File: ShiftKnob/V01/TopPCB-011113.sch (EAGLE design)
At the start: 6 parts, among them IC1 74HC595D

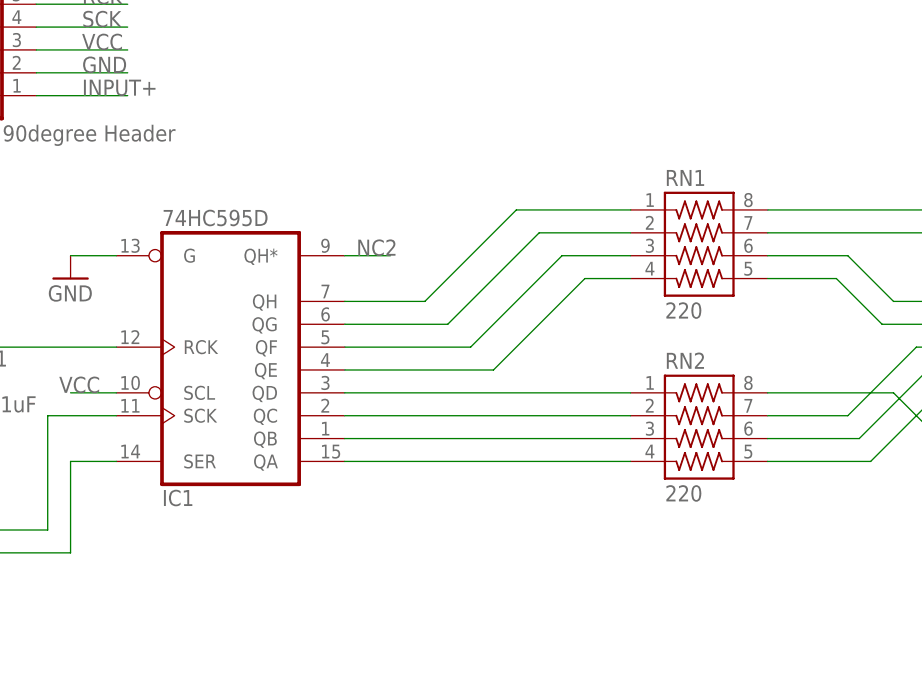
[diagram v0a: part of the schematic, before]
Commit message: name components, add silk screen labels, copy name-date-logo to bottom layer, increase board diameter to 33mm
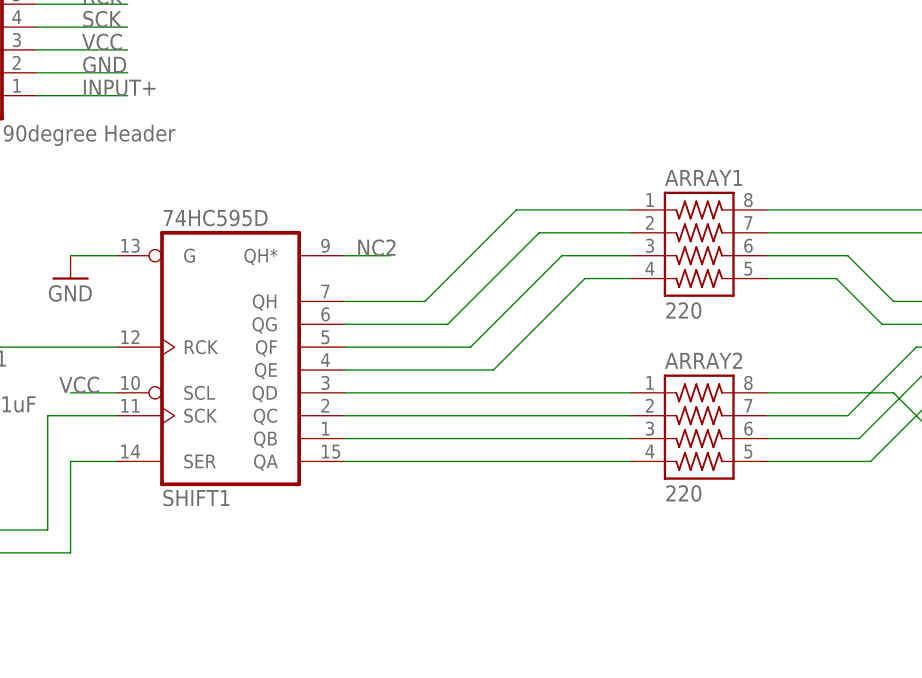
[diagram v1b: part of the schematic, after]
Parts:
- renumbered IC1 to SHIFT1, RN1 to ARRAY1, RN2 to ARRAY2, U$1 to 7SEGMENT

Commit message: change 6 pin connector to match bottomPCB. run DRC and correct issues. move dimension callout to Document layer.
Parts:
- JP1: device SparkFun-Connectors:M06POGOPIN_HOLES_ONLY -> SparkFun-Connectors:M06SIP
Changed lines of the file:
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@@
 <part name="FRAME1" library="frames" deviceset="FRAME_A_L" device=""/>
 <part name="GND3" library="SparkFun-Aesthetics" deviceset="GND" device=""/>
-<part name="JP1" library="SparkFun-Connectors" deviceset="M06" device="POGOPIN_HOLES_ONLY" value="6 PIN 90degree Header"/>
+<part name="JP1" library="SparkFun-Connectors" deviceset="M06" device="SIP" value="6 PIN 90degree Header"/>
 <part name="C1" library="SparkFun-Capacitors" deviceset="CAP" device="0402-CAP" value="0.1uF"/>
 <part name="GND4" library="SparkFun-Aesthetics" deviceset="GND" device=""/>

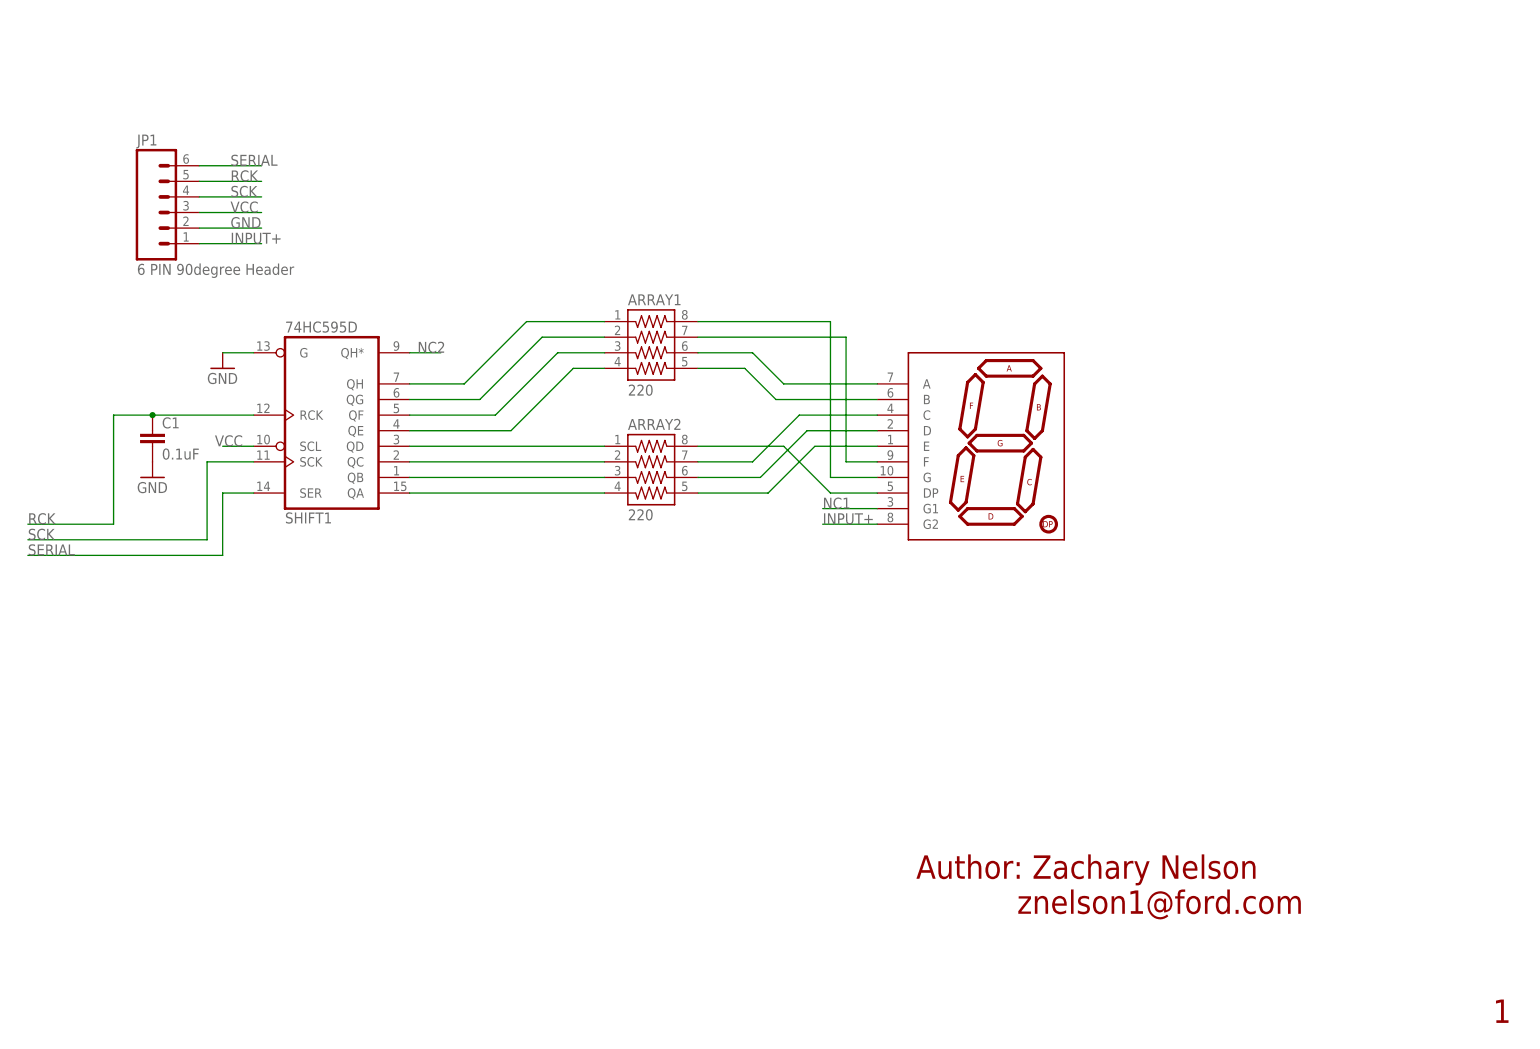
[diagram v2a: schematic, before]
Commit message: update schematics with new Ford frame.
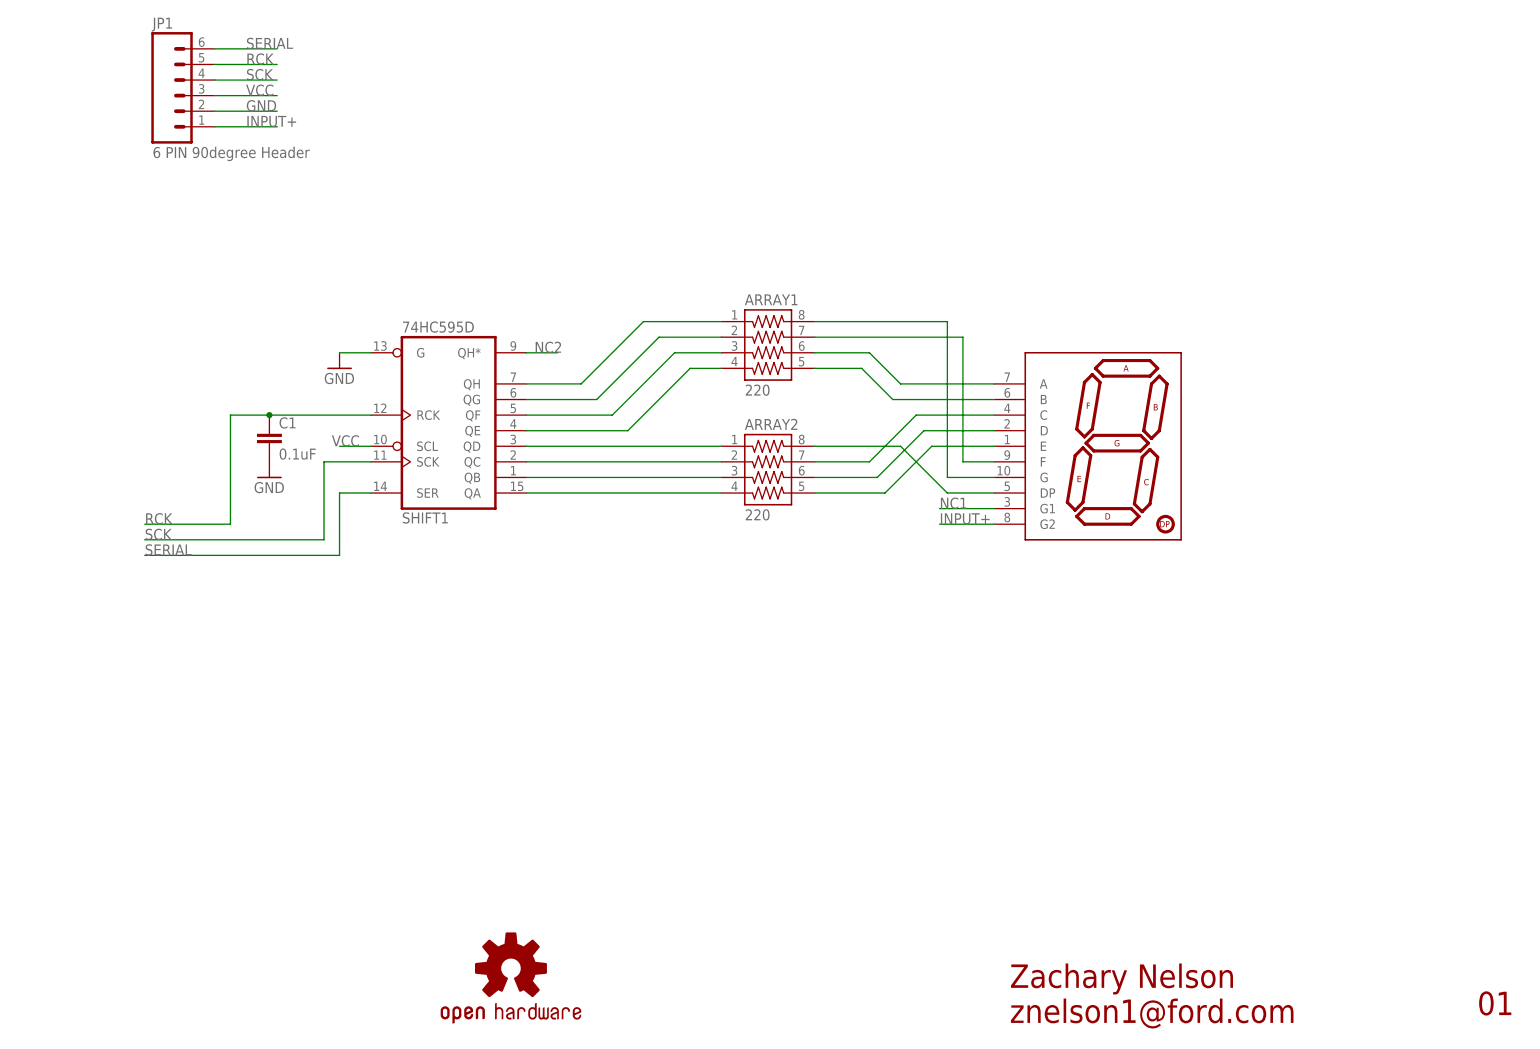
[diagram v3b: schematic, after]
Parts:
- added LOGO1: OSHW-LOGOS, SparkFun-Aesthetics:OSHW-LOGOS
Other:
- note added: "01"
- note added: "Zachary Nelson znelson1@ford.com"
- note removed: "1"
- note removed: "Author: Zachary Nelson znelson1@ford.com"
- moved on the sheet: ARRAY1, ARRAY2, C1, JP1, SHIFT1

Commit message: update with new frames and printed drawings for assembly.
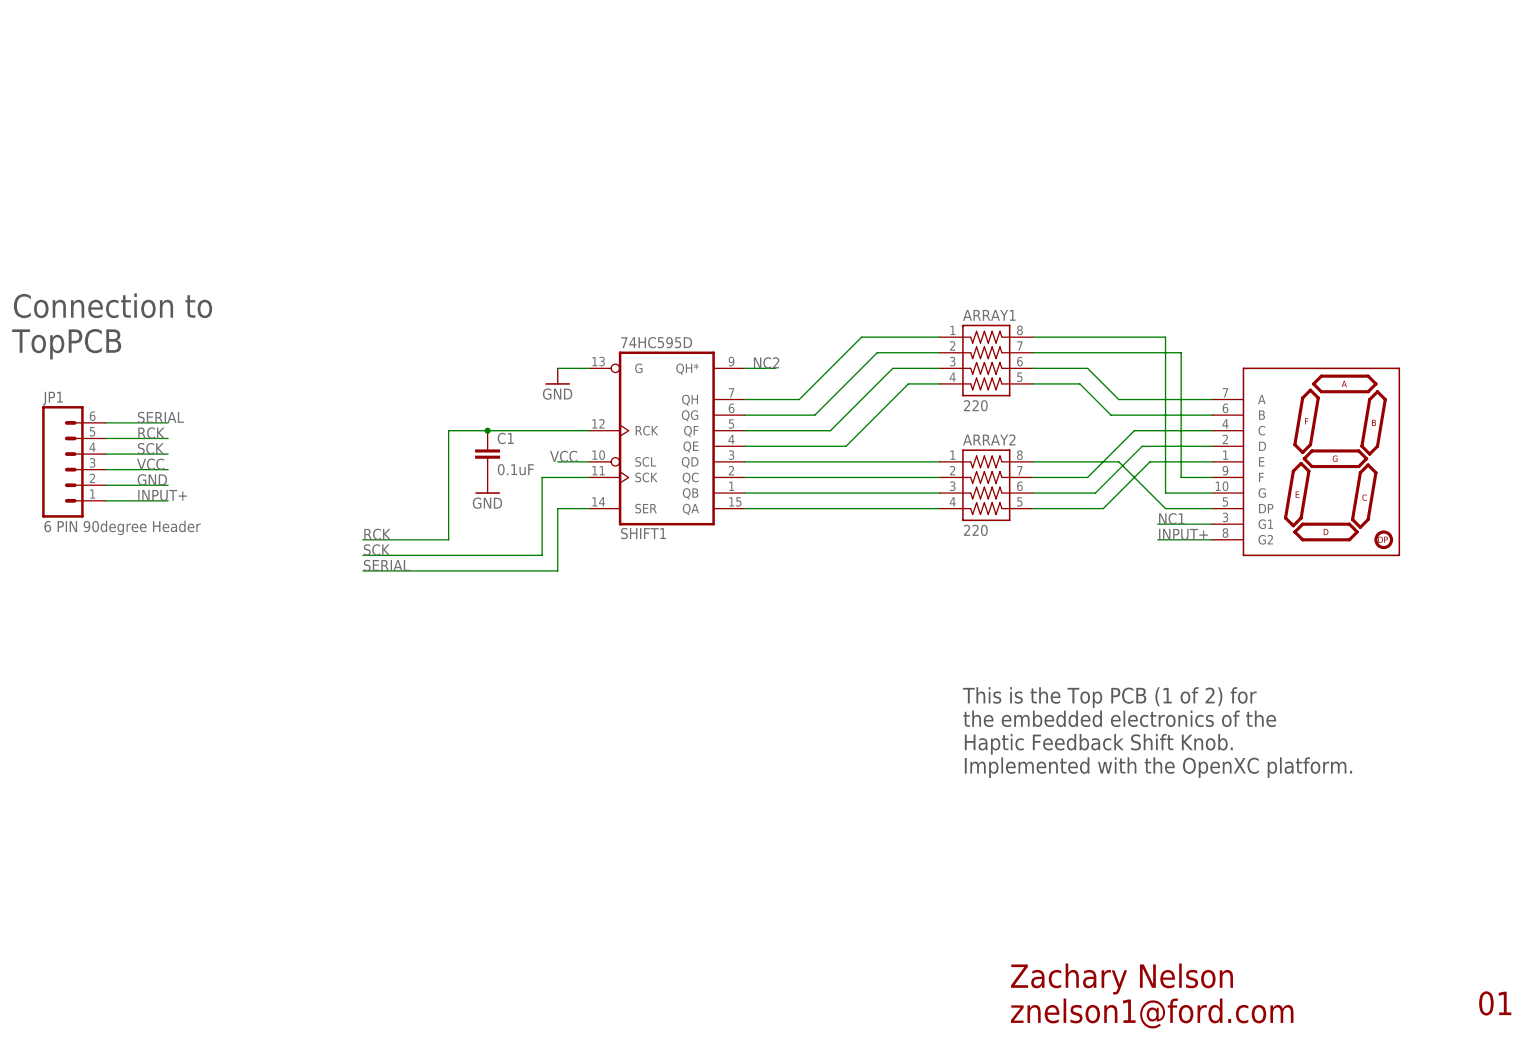
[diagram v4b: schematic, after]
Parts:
- removed LOGO1: OSHW-LOGOS, SparkFun-Aesthetics:OSHW-LOGOS
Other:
- note added: "Connection to TopPCB"
- note added: "This is the Top PCB (1 of 2) for the embedded electronics of the Haptic Feedback Shift Knob. Implemented with the OpenXC platform."
- moved on the sheet: ARRAY1, ARRAY2, C1, JP1, SHIFT1
